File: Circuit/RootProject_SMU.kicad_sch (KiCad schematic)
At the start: 2 parts, among them J2 MJ-179PH

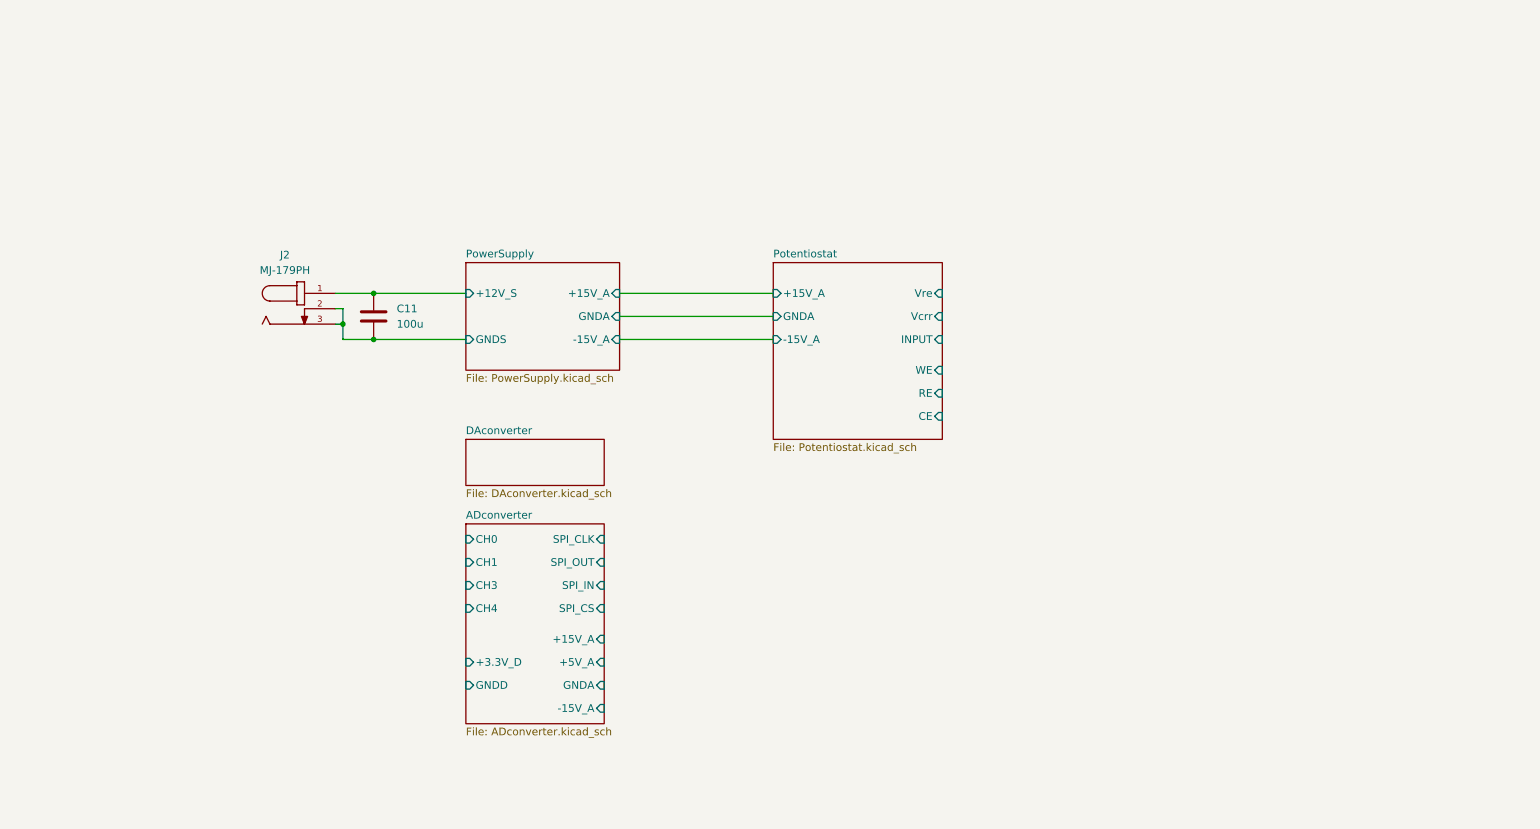
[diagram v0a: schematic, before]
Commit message: SMUの各部分の配線を追加
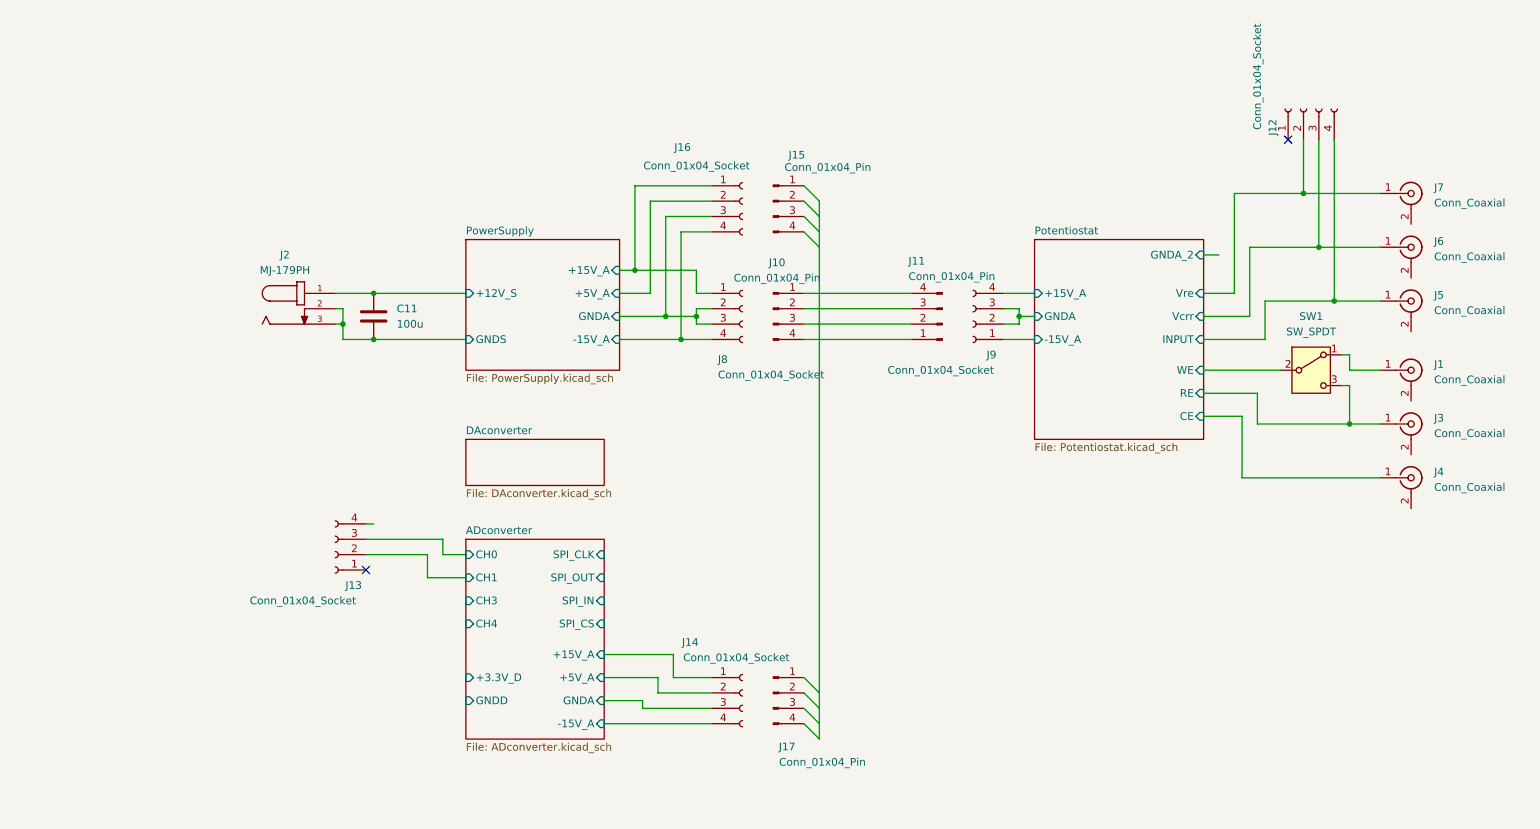
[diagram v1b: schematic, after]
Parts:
- added J1, J3, J4, J5, J6, J7: Conn_Coaxial, symbol Connector:Conn_Coaxial
- added J10, J11, J16, J17: Conn_01x04_Pin, symbol Connector:Conn_01x04_Pin
- added J12, J13, J14, J15, J8, J9: Conn_01x04_Socket, symbol Connector:Conn_01x04_Socket
- added SW1: SW_SPDT, symbol Switch:SW_SPDT
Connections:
- net ADconverter/+15V_A: now also J14.1 (Pin_1)
- net ADconverter/+5V_A: now also J14.2 (Pin_2)
- net ADconverter/-15V_A: now also J14.4 (Pin_4)
- net ADconverter/CH0: now also J13.3 (Pin_3)
- net ADconverter/CH1: now also J13.2 (Pin_2)
- net ADconverter/GNDA: now also J14.3 (Pin_3)
- net Potentiostat/+15V_A: now also J9.4 (Pin_4)
- net Potentiostat/-15V_A: now also J9.1 (Pin_1)
- net Potentiostat/CE: now also J4.1 (In)
- net Potentiostat/GNDA: now also J9.2 (Pin_2), J9.3 (Pin_3)
- net Potentiostat/INPUT: now also J12.4 (Pin_4), J5.1 (In)
- net Potentiostat/RE: now also J3.1 (In), SW1.3 (C)
- net Potentiostat/Vcrr: now also J12.3 (Pin_3), J6.1 (In)
- net Potentiostat/Vre: now also J12.2 (Pin_2), J7.1 (In)
- net Potentiostat/WE: now also SW1.2 (B)
- new net: J10.4 (Pin_4), J11.1 (Pin_1)
- new net: J10.3 (Pin_3), J11.2 (Pin_2)
- new net: J10.2 (Pin_2), J11.3 (Pin_3)
- new net: J10.1 (Pin_1), J11.4 (Pin_4)
- new net: J1.1 (In), SW1.1 (A)
- new net PowerSupply/+15V_A: J15.1 (Pin_1), J8.1 (Pin_1)
- new net PowerSupply/+5V_A: J15.2 (Pin_2)
- new net PowerSupply/-15V_A: J15.4 (Pin_4), J8.4 (Pin_4)
- new net PowerSupply/GNDA: J15.3 (Pin_3), J8.2 (Pin_2), J8.3 (Pin_3)
- no-connect marks 0 -> 2
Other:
- sheet Potentiostat ports: added GNDA_2; removed none
- sheet PowerSupply ports: added +5V_A; removed none

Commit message: 各部品の配線が完了。部品表を作り、発注書を作成。
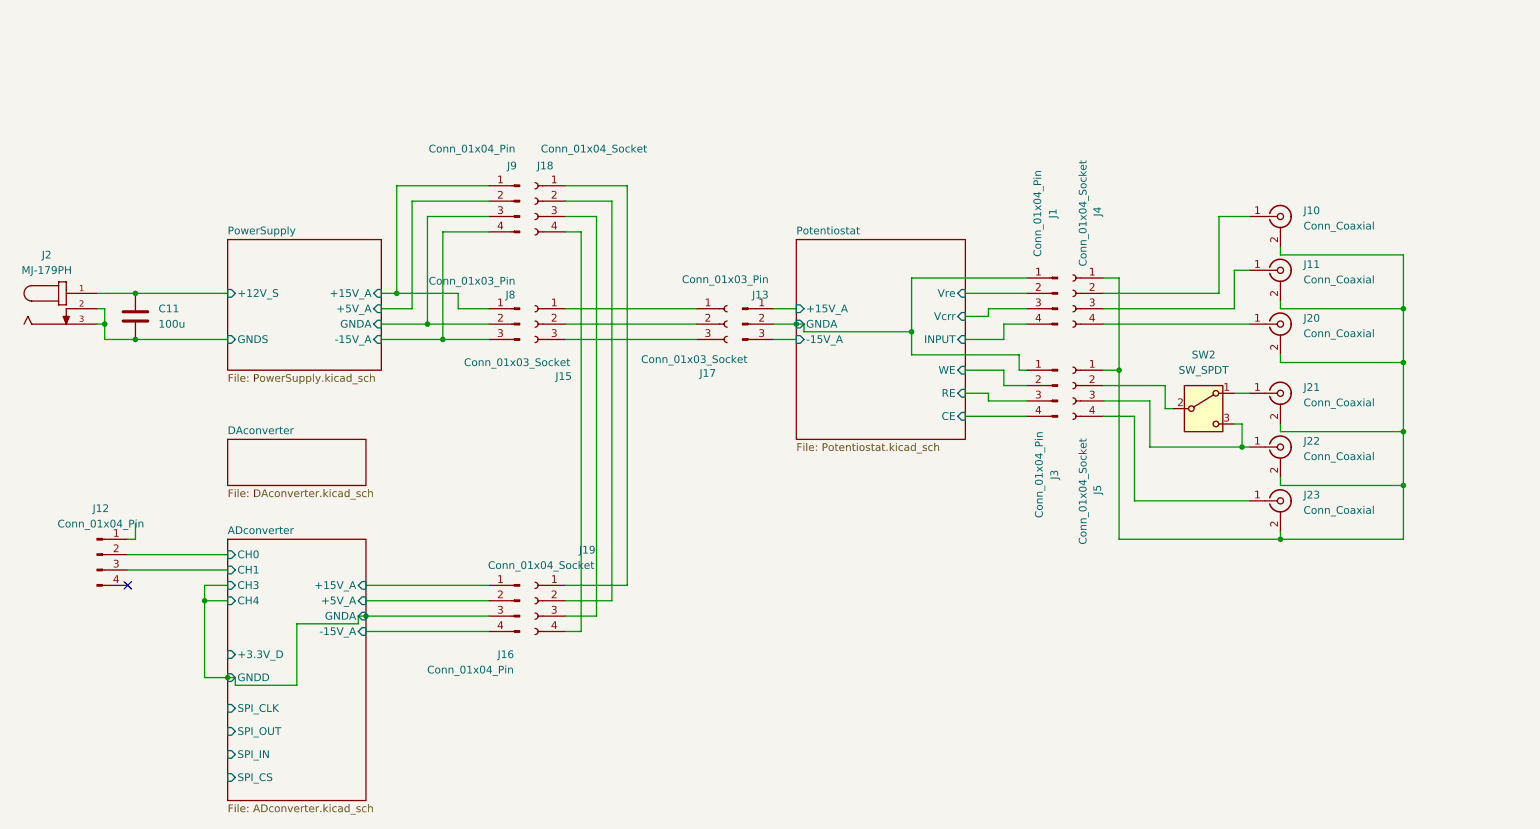
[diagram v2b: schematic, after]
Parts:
- removed J1, J3, J4, J5, J6, J7: Conn_Coaxial, symbol Connector:Conn_Coaxial
- removed J10, J11, J17: Conn_01x04_Pin, symbol Connector:Conn_01x04_Pin
- removed J12, J13, J14, J15, J8, J9: Conn_01x04_Socket, symbol Connector:Conn_01x04_Socket
- removed SW1: SW_SPDT, symbol Switch:SW_SPDT
- added J1, J12, J3, J9: Conn_01x04_Pin, symbol Connector:Conn_01x04_Pin
- added J10, J11, J20, J21, J22, J23: Conn_Coaxial, symbol Connector:Conn_Coaxial
- added J13, J8: Conn_01x03_Pin, symbol Connector:Conn_01x03_Pin
- added J15, J17: Conn_01x03_Socket, symbol Connector:Conn_01x03_Socket
- added J18, J19, J4, J5: Conn_01x04_Socket, symbol Connector:Conn_01x04_Socket
- added SW2: SW_SPDT, symbol Switch:SW_SPDT
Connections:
- net ADconverter/+15V_A: now also J16.1 (Pin_1)
- net ADconverter/+5V_A: now also J16.2 (Pin_2)
- net ADconverter/-15V_A: now also J16.4 (Pin_4)
- net ADconverter/CH0: now also J12.2 (Pin_2)
- net ADconverter/CH1: now also J12.3 (Pin_3)
- net ADconverter/CH3: now also J16.3 (Pin_3)
- net Potentiostat/+15V_A: now also J13.1 (Pin_1)
- net Potentiostat/-15V_A: now also J13.3 (Pin_3)
- net Potentiostat/CE: now also J3.4 (Pin_4)
- net Potentiostat/GNDA: now also J1.1 (Pin_1), J13.2 (Pin_2), J3.1 (Pin_1)
- net Potentiostat/INPUT: now also J1.4 (Pin_4)
- net Potentiostat/RE: now also J3.3 (Pin_3)
- net Potentiostat/Vcrr: now also J1.3 (Pin_3)
- net Potentiostat/Vre: now also J1.2 (Pin_2)
- net Potentiostat/WE: now also J3.2 (Pin_2)
- net PowerSupply/+15V_A: now also J8.1 (Pin_1), J9.1 (Pin_1)
- net PowerSupply/+5V_A: now also J9.2 (Pin_2)
- net PowerSupply/-15V_A: now also J8.3 (Pin_3), J9.4 (Pin_4)
- net PowerSupply/GNDA: now also J8.2 (Pin_2), J9.3 (Pin_3)
- new net: J18.1 (Pin_1), J19.1 (Pin_1)
- new net: J18.2 (Pin_2), J19.2 (Pin_2)
- new net: J18.3 (Pin_3), J19.3 (Pin_3)
- new net: J18.4 (Pin_4), J19.4 (Pin_4)
- new net: J15.1 (Pin_1), J17.1 (Pin_1)
- new net: J15.2 (Pin_2), J17.2 (Pin_2)
- new net: J15.3 (Pin_3), J17.3 (Pin_3)
- new net: J10.2 (Ext), J11.2 (Ext), J20.2 (Ext), J21.2 (Ext), J22.2 (Ext), J23.2 (Ext), J4.1 (Pin_1), J5.1 (Pin_1)
- new net: J5.2 (Pin_2), SW2.2 (B)
- new net: J22.1 (In), J5.3 (Pin_3), SW2.3 (C)
- new net: J23.1 (In), J5.4 (Pin_4)
- new net: J11.1 (In), J4.3 (Pin_3)
- new net: J20.1 (In), J4.4 (Pin_4)
- new net: J10.1 (In), J4.2 (Pin_2)
- new net: J21.1 (In), SW2.1 (A)
- no-connect marks 2 -> 1
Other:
- sheet Potentiostat ports: added none; removed GNDA_2
- moved on the sheet: C11, J2

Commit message: 更新
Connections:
- net Potentiostat/RE: now also J3.2 (Pin_2); no longer J3.3 (Pin_3)
- net Potentiostat/WE: now also J3.3 (Pin_3); no longer J3.2 (Pin_2)
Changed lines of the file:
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@@
+	(wire
+		(pts
+			(xy 181.61 91.44) (xy 185.42 91.44)
+		)
+		(stroke
+			(width 0)
+			(type default)
+		)
+	)
 	(wire
 		(pts
@@
 	(wire
 		(pts
-			(xy 181.61 91.44) (xy 185.42 91.44)
-		)
-		(stroke
-			(width 0)
-			(type default)
-		)
-	)
-	(wire
-		(pts
 			(xy 185.42 77.47) (xy 191.77 77.47)
 		)
@@
 	(wire
 		(pts
+			(xy 226.06 91.44) (xy 228.6 91.44)
+		)
+		(stroke
+			(width 0)
+			(type default)
+		)
+	)
+	(wire
+		(pts
+			(xy 227.33 100.33) (xy 227.33 96.52)
+		)
+		(stroke
+			(width 0)
+			(type default)
+		)
+	)
+	(wire
+		(pts
+			(xy 120.65 62.23) (xy 120.65 128.27)
+		)
+		(stroke
+			(width 0)
+			(type default)
+		)
+	)
+	(wire
+		(pts
+			(xy 212.09 92.71) (xy 212.09 100.33)
+		)
+		(stroke
+			(width 0)
+			(type default)
+		)
+	)
+	(wire
+		(pts
+			(xy 59.69 138.43) (xy 60.96 138.43)
+		)
+		(stroke
+			(width 0)
+			(type default)
+		)
+	)
+	(wire
+		(pts
+			(xy 187.96 80.01) (xy 187.96 82.55)
+		)
+		(stroke
+			(width 0)
+			(type default)
+		)
+	)
+	(wire
+		(pts
+			(xy 43.18 120.65) (xy 59.69 120.65)
+		)
+		(stroke
+			(width 0)
+			(type default)
+		)
+	)
+	(wire
+		(pts
+			(xy 226.06 71.12) (xy 228.6 71.12)
+		)
+		(stroke
+			(width 0)
+			(type default)
+		)
+	)
+	(wire
+		(pts
+			(xy 85.09 82.55) (xy 95.25 82.55)
+		)
+		(stroke
+			(width 0)
+			(type default)
+		)
+	)
+	(wire
+		(pts
+			(xy 95.25 64.77) (xy 95.25 82.55)
+		)
+		(stroke
+			(width 0)
+			(type default)
+		)
+	)
+	(wire
+		(pts
+			(xy 60.96 139.7) (xy 71.12 139.7)
+		)
+		(stroke
+			(width 0)
+			(type default)
+		)
+	)
+	(wire
+		(pts
+			(xy 154.94 81.28) (xy 172.72 81.28)
+		)
+		(stroke
+			(width 0)
+			(type default)
+		)
+	)
+	(wire
+		(pts
 			(xy 181.61 87.63) (xy 187.96 87.63)
-		)
-		(stroke
-			(width 0)
-			(type default)
-		)
-	)
-	(wire
-		(pts
-			(xy 226.06 91.44) (xy 228.6 91.44)
-		)
-		(stroke
-			(width 0)
-			(type default)
-		)
-	)
-	(wire
-		(pts
-			(xy 227.33 100.33) (xy 227.33 96.52)
-		)
-		(stroke
-			(width 0)
-			(type default)
-		)
-	)
-	(wire
-		(pts
-			(xy 120.65 62.23) (xy 120.65 128.27)
-		)
-		(stroke
-			(width 0)
-			(type default)
-		)
-	)
-	(wire
-		(pts
-			(xy 212.09 92.71) (xy 212.09 100.33)
-		)
-		(stroke
-			(width 0)
-			(type default)
-		)
-	)
-	(wire
-		(pts
-			(xy 59.69 138.43) (xy 60.96 138.43)
-		)
-		(stroke
-			(width 0)
-			(type default)
-		)
-	)
-	(wire
-		(pts
-			(xy 187.96 80.01) (xy 187.96 82.55)
-		)
-		(stroke
-			(width 0)
-			(type default)
-		)
-	)
-	(wire
-		(pts
-			(xy 43.18 120.65) (xy 59.69 120.65)
-		)
-		(stroke
-			(width 0)
-			(type default)
-		)
-	)
-	(wire
-		(pts
-			(xy 226.06 71.12) (xy 228.6 71.12)
-		)
-		(stroke
-			(width 0)
-			(type default)
-		)
-	)
-	(wire
-		(pts
-			(xy 85.09 82.55) (xy 95.25 82.55)
-		)
-		(stroke
-			(width 0)
-			(type default)
-		)
-	)
-	(wire
-		(pts
-			(xy 95.25 64.77) (xy 95.25 82.55)
-		)
-		(stroke
-			(width 0)
-			(type default)
-		)
-	)
-	(wire
-		(pts
-			(xy 60.96 139.7) (xy 71.12 139.7)
-		)
-		(stroke
-			(width 0)
-			(type default)
-		)
-	)
-	(wire
-		(pts
-			(xy 154.94 81.28) (xy 172.72 81.28)
 		)
 		(stroke
@@
 		)
 		(pin "RE" input
+			(at 181.61 87.63 0)
+			(effects
+				(font
+					(size 1.27 1.27)
+				)
+				(justify right)
+			)
+		)
+		(pin "WE" input
 			(at 181.61 91.44 0)
 			(effects
 				(font
-					(size 1.27 1.27)
-				)
-				(justify right)
-			)
-		)
-		(pin "WE" input
-			(at 181.61 87.63 0)
-			(effects
-				(font
